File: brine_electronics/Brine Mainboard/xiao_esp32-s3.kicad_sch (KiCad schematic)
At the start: 4 parts, among them U1 XIAO-ESP32-S3-SMD

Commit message: Updated electronics/enclosure designs
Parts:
- removed H3: Antenna, MountingHole:MountingHole_3.2mm_M3, symbol Mechanical:MountingHole
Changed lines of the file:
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@@
-	)
-	(symbol
-		(lib_id "Mechanical:MountingHole")
-		(at 114.3 127 0)
-		(unit 1)
-		(exclude_from_sim yes)
-		(in_bom no)
-		(on_board yes)
-		(dnp no)
-		(fields_autoplaced yes)
-		(property "Reference" "H3"
-			(at 116.84 125.7299 0)
-			(effects
-				(font
-					(size 1.27 1.27)
-				)
-				(justify left)
-			)
-		)
-		(property "Value" "Antenna"
-			(at 116.84 128.2699 0)
-			(effects
-				(font
-					(size 1.27 1.27)
-				)
-				(justify left)
-			)
-		)
-		(property "Footprint" "MountingHole:MountingHole_3.2mm_M3"
-			(at 114.3 127 0)
-			(effects
-				(font
-					(size 1.27 1.27)
-				)
-				(hide yes)
-			)
-		)
-		(property "Datasheet" "~"
-			(at 114.3 127 0)
-			(effects
-				(font
-					(size 1.27 1.27)
-				)
-				(hide yes)
-			)
-		)
-		(property "Description" "Mounting Hole without connection"
-			(at 114.3 127 0)
-			(effects
-				(font
-					(size 1.27 1.27)
-				)
-				(hide yes)
-			)
-		)
-		(instances
-			(project "Brine"
-				(path "/da3a4ef2-0e38-46f1-a1fc-55d8e0a83a54/63bc593b-afd3-4a61-9e23-7e85a1d104e9"
-					(reference "H3")
-					(unit 1)
-				)
-			)
-		)
 	)
 	(symbol

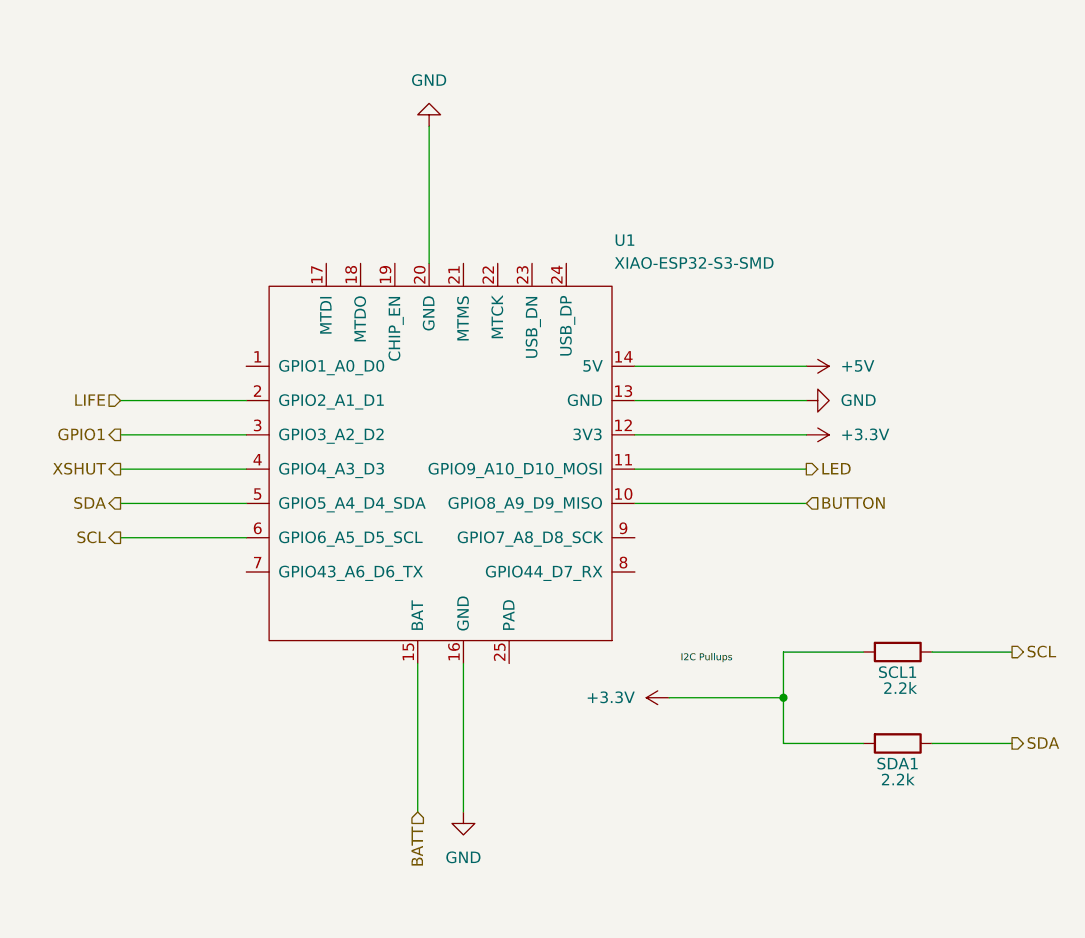
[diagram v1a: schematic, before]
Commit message: Implemented power latch circuit ⚡
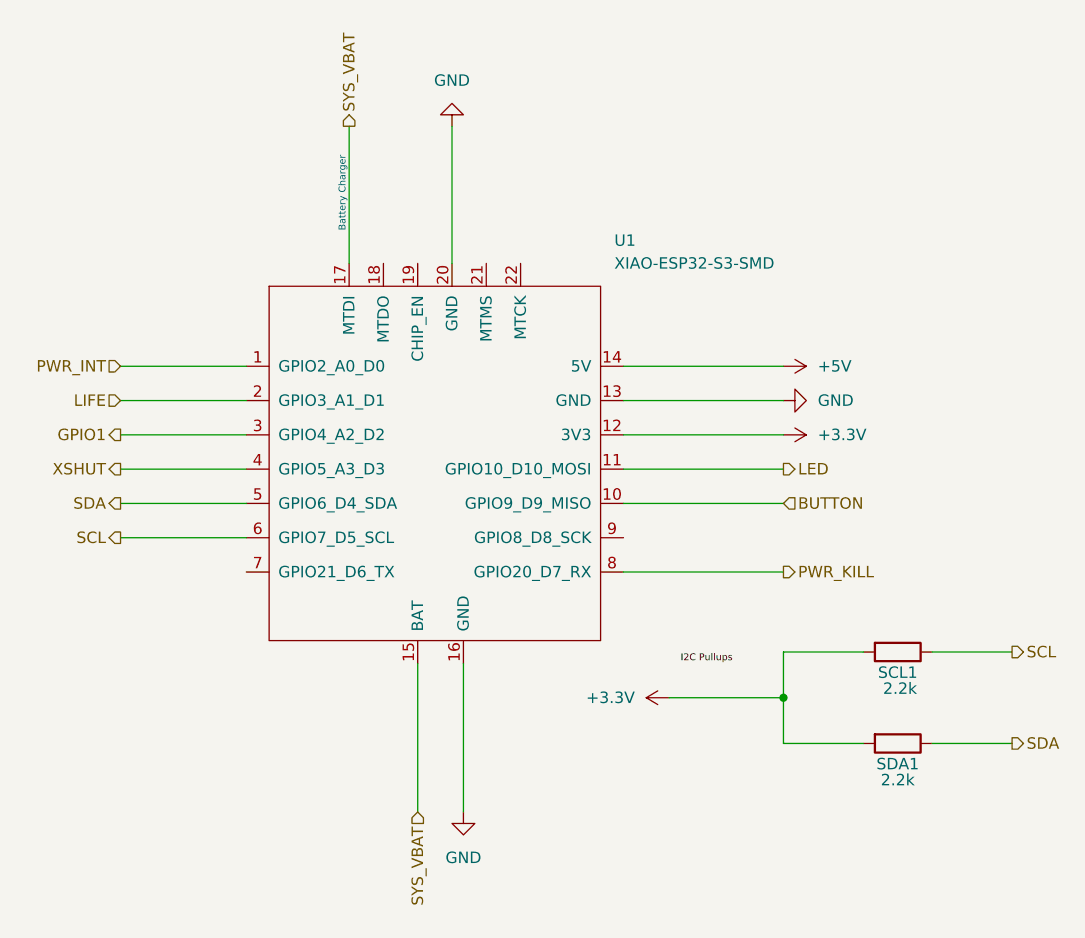
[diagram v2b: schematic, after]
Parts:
- U1: symbol Seeed_Studio_XIAO_Series:XIAO-ESP32-S3-SMD -> Seeed_Studio_XIAO_Series:XIAO-ESP32-C3-SMD
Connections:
- net BATT is gone; now on net SYS_VBAT: U1.15 (BAT)
- net PWR_INT: now reaches U1.1 (GPIO2_A0_D0)
- net SYS_VBAT: now reaches U1.17 (MTDI)
- net PWR_KILL: now reaches U1.8 (GPIO20_D7_RX)
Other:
- note added: "Battery Charger"
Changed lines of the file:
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@@
 		(comment 2 "The module incorporates a battery charger.")
+	)
+	(text "Battery Charger"
+		(exclude_from_sim no)
+		(at 128.778 71.12 90)
+		(effects
+			(font
+				(size 0.762 0.762)
+			)
+		)
 	)
 	(junction
@@
 	(wire
 		(pts
-			(xy 161.29 101.6) (xy 180.34 101.6)
-		)
-		(stroke
-			(width 0)
-			(type default)
-		)
-	)
-	(wire
-		(pts
 			(xy 142.24 123.19) (xy 142.24 139.7)
 		)
@@
 	(wire
 		(pts
-			(xy 161.29 105.41) (xy 180.34 105.41)
+			(xy 160.02 101.6) (xy 177.8 101.6)
+		)
+		(stroke
+			(width 0)
+			(type default)
+		)
+	)
+	(wire
+		(pts
+			(xy 160.02 93.98) (xy 177.8 93.98)
+		)
+		(stroke
+			(width 0)
+			(type default)
+		)
+	)
+	(wire
+		(pts
+			(xy 160.02 113.03) (xy 177.8 113.03)
 		)
 		(stroke
@@
 	(wire
 		(pts
-			(xy 161.29 93.98) (xy 180.34 93.98)
-		)
-		(stroke
-			(width 0)
-			(type default)
-		)
-	)
-	(wire
-		(pts
 			(xy 104.14 101.6) (xy 118.11 101.6)
 		)
@@
 	(wire
 		(pts
-			(xy 138.43 63.5) (xy 138.43 78.74)
+			(xy 140.97 63.5) (xy 140.97 78.74)
 		)
 		(stroke
@@
 	(wire
 		(pts
-			(xy 161.29 90.17) (xy 180.34 90.17)
+			(xy 129.54 63.5) (xy 129.54 78.74)
+		)
+		(stroke
+			(width 0)
+			(type default)
+		)
+	)
+	(wire
+		(pts
+			(xy 160.02 90.17) (xy 177.8 90.17)
+		)
+		(stroke
+			(width 0)
+			(type default)
+		)
+	)
+	(wire
+		(pts
+			(xy 104.14 90.17) (xy 118.11 90.17)
 		)
 		(stroke
@@
 	(wire
 		(pts
-			(xy 161.29 97.79) (xy 180.34 97.79)
+			(xy 160.02 97.79) (xy 177.8 97.79)
+		)
+		(stroke
+			(width 0)
+			(type default)
+		)
+	)
+	(wire
+		(pts
+			(xy 160.02 105.41) (xy 177.8 105.41)
 		)
 		(stroke
@@
 	(hierarchical_label "BUTTON"
 		(shape input)
-		(at 180.34 105.41 0)
+		(at 177.8 105.41 0)
 		(effects
 			(font
@@
 		)
 	)
+	(hierarchical_label "PWR_INT"
+		(shape input)
+		(at 104.14 90.17 180)
+		(effects
+			(font
+				(size 1.27 1.27)
+			)
+			(justify right)
+		)
+	)
 	(hierarchical_label "GPIO1"
 		(shape output)
@@
 		)
 	)
+	(hierarchical_label "SYS_VBAT"
+		(shape output)
+		(at 129.54 63.5 90)
+		(effects
+			(font
+				(size 1.27 1.27)
+			)
+			(justify left)
+		)
+	)
+	(hierarchical_label "PWR_KILL"
+		(shape output)
+		(at 177.8 113.03 0)
+		(effects
+			(font
+				(size 1.27 1.27)
+			)
+			(justify left)
+		)
+	)
 	(hierarchical_label "SCL"
 		(shape output)
@@
 		)
 	)
-	(hierarchical_label "BATT"
+	(hierarchical_label "SYS_VBAT"
 		(shape input)
 		(at 137.16 139.7 270)
@@
 	(hierarchical_label "LED"
 		(shape output)
-		(at 180.34 101.6 0)
+		(at 177.8 101.6 0)
 		(effects
 			(font
@@
 	)
 	(symbol
-		(lib_id "Seeed_Studio_XIAO_Series:XIAO-ESP32-S3-SMD")
+		(lib_id "Seeed_Studio_XIAO_Series:XIAO-ESP32-C3-SMD")
 		(at 139.7 101.6 0)
 		(unit 1)
@@
 		(pin "13"
 		)
-		(pin "23"
-		)
 		(pin "16"
 		)
@@
 		(pin "14"
 		)
-		(pin "24"
-		)
 		(pin "21"
 		)
@@
 		)
 		(pin "11"
-		)
-		(pin "25"
 		)
 		(instances
@@
 	(symbol
 		(lib_id "power:+3.3V")
-		(at 180.34 97.79 270)
+		(at 177.8 97.79 270)
 		(unit 1)
 		(exclude_from_sim no)
@@
 		(fields_autoplaced yes)
 		(property "Reference" "#PWR03"
-			(at 176.53 97.79 0)
+			(at 173.99 97.79 0)
 			(effects
 				(font
@@
 		)
 		(property "Value" "+3.3V"
-			(at 184.15 97.7899 90)
+			(at 181.61 97.7899 90)
 			(effects
 				(font
@@
 		)
 		(property "Footprint" ""
-			(at 180.34 97.79 0)
+			(at 177.8 97.79 0)
 			(effects
 				(font
@@
 		)
 		(property "Datasheet" ""
-			(at 180.34 97.79 0)
+			(at 177.8 97.79 0)
 			(effects
 				(font
@@
 		)
 		(property "Description" "Power symbol creates a global label with name \"+3.3V\""
-			(at 180.34 97.79 0)
+			(at 177.8 97.79 0)
 			(effects
 				(font
@@
 	(symbol
 		(lib_id "power:+5V")
-		(at 180.34 90.17 270)
+		(at 177.8 90.17 270)
 		(unit 1)
 		(exclude_from_sim no)
@@
 		(fields_autoplaced yes)
 		(property "Reference" "#PWR010"
-			(at 176.53 90.17 0)
+			(at 173.99 90.17 0)
 			(effects
 				(font
@@
 		)
 		(property "Value" "+5V"
-			(at 184.15 90.1699 90)
+			(at 181.61 90.1699 90)
 			(effects
 				(font
@@
 		)
 		(property "Footprint" ""
-			(at 180.34 90.17 0)
+			(at 177.8 90.17 0)
 			(effects
 				(font
@@
 		)
 		(property "Datasheet" ""
-			(at 180.34 90.17 0)
+			(at 177.8 90.17 0)
 			(effects
 				(font
@@
 		)
 		(property "Description" "Power symbol creates a global label with name \"+5V\""
-			(at 180.34 90.17 0)
+			(at 177.8 90.17 0)
 			(effects
 				(font
@@
 	(symbol
 		(lib_id "power:GND")
-		(at 138.43 63.5 180)
+		(at 140.97 63.5 180)
 		(unit 1)
 		(exclude_from_sim no)
@@
 		(fields_autoplaced yes)
 		(property "Reference" "#PWR04"
-			(at 138.43 57.15 0)
+			(at 140.97 57.15 0)
 			(effects
 				(font
@@
 		)
 		(property "Value" "GND"
-			(at 138.43 58.42 0)
+			(at 140.97 58.42 0)
 			(effects
 				(font
@@
 		)
 		(property "Footprint" ""
-			(at 138.43 63.5 0)
+			(at 140.97 63.5 0)
 			(effects
 				(font
@@
 		)
 		(property "Datasheet" ""
-			(at 138.43 63.5 0)
+			(at 140.97 63.5 0)
 			(effects
 				(font
@@
 		)
 		(property "Description" "Power symbol creates a global label with name \"GND\" , ground"
-			(at 138.43 63.5 0)
+			(at 140.97 63.5 0)
 			(effects
 				(font
@@
 	(symbol
 		(lib_id "power:GND")
-		(at 180.34 93.98 90)
+		(at 177.8 93.98 90)
 		(unit 1)
 		(exclude_from_sim no)
@@
 		(fields_autoplaced yes)
 		(property "Reference" "#PWR02"
-			(at 186.69 93.98 0)
+			(at 184.15 93.98 0)
 			(effects
 				(font
@@
 		)
 		(property "Value" "GND"
-			(at 184.15 93.9799 90)
+			(at 181.61 93.9799 90)
 			(effects
 				(font
@@
 		)
 		(property "Footprint" ""
-			(at 180.34 93.98 0)
+			(at 177.8 93.98 0)
 			(effects
 				(font
@@
 		)
 		(property "Datasheet" ""
-			(at 180.34 93.98 0)
+			(at 177.8 93.98 0)
 			(effects
 				(font
@@
 		)
 		(property "Description" "Power symbol creates a global label with name \"GND\" , ground"
-			(at 180.34 93.98 0)
-			(effects
-				(font
+			(at 177.8 93.98 0)
+			(effects
+				(font

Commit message: Resolved schematic DRC issues ✅
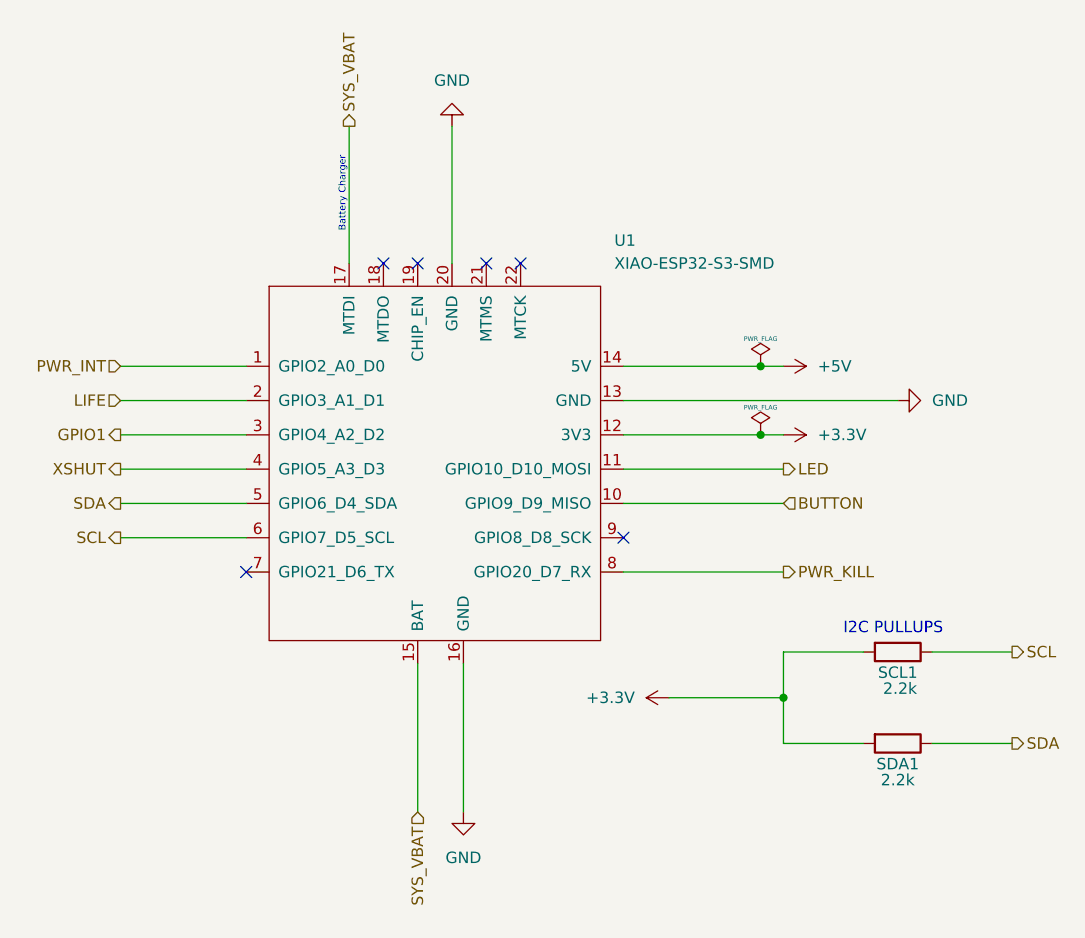
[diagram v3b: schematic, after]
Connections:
- no-connect marks 0 -> 6
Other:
- note added: "I2C PULLUPS"
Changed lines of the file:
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@@
 	(title_block
 		(title "Brine - XIAO ESP32-S3")
-		(date "2026-04-03")
+		(date "2026-04-07")
 		(rev "1.0.0")
 		(company "Splendid Endeavors")
@@
 		(comment 2 "The module incorporates a battery charger.")
 	)
+	(text "I2C PULLUPS"
+		(exclude_from_sim no)
+		(at 189.992 119.38 0)
+		(effects
+			(font
+				(size 1.27 1.27)
+			)
+		)
+	)
 	(text "Battery Charger"
 		(exclude_from_sim no)
@@
 			)
 		)
+	)
+	(junction
+		(at 175.26 90.17)
+		(diameter 0)
+		(color 0 0 0 0)
+	)
+	(junction
+		(at 175.26 97.79)
+		(diameter 0)
+		(color 0 0 0 0)
 	)
 	(junction
@@
 		(color 0 0 0 0)
 	)
+	(no_connect
+		(at 148.59 78.74)
+	)
+	(no_connect
+		(at 137.16 78.74)
+	)
+	(no_connect
+		(at 160.02 109.22)
+	)
+	(no_connect
+		(at 118.11 113.03)
+	)
+	(no_connect
+		(at 144.78 78.74)
+	)
+	(no_connect
+		(at 133.35 78.74)
+	)
 	(wire
 		(pts
@@
 	(wire
 		(pts
-			(xy 160.02 93.98) (xy 177.8 93.98)
+			(xy 160.02 93.98) (xy 190.5 93.98)
 		)
 		(stroke
@@
 	(wire
 		(pts
+			(xy 175.26 90.17) (xy 177.8 90.17)
+		)
+		(stroke
+			(width 0)
+			(type default)
+		)
+	)
+	(wire
+		(pts
 			(xy 104.14 93.98) (xy 118.11 93.98)
 		)
@@
 	(wire
 		(pts
-			(xy 160.02 90.17) (xy 177.8 90.17)
+			(xy 175.26 97.79) (xy 177.8 97.79)
+		)
+		(stroke
+			(width 0)
+			(type default)
+		)
+	)
+	(wire
+		(pts
+			(xy 160.02 90.17) (xy 175.26 90.17)
 		)
 		(stroke
@@
 	(wire
 		(pts
-			(xy 160.02 97.79) (xy 177.8 97.79)
+			(xy 160.02 97.79) (xy 175.26 97.79)
 		)
 		(stroke
@@
 			(width 0)
 			(type default)
-		)
-	)
-	(label "I2C Pullups"
-		(at 166.37 123.19 0)
-		(effects
-			(font
-				(size 0.762 0.762)
-			)
-			(justify left bottom)
 		)
 	)
@@
 	)
 	(symbol
+		(lib_id "power:PWR_FLAG")
+		(at 175.26 90.17 0)
+		(unit 1)
+		(exclude_from_sim no)
+		(in_bom yes)
+		(on_board yes)
+		(dnp no)
+		(property "Reference" "#FLG01"
+			(at 175.26 88.265 0)
+			(effects
+				(font
+					(size 1.27 1.27)
+				)
+				(hide yes)
+			)
+		)
+		(property "Value" "PWR_FLAG"
+			(at 175.26 87.122 0)
+			(effects
+				(font
+					(size 0.508 0.508)
+				)
+			)
+		)
+		(property "Footprint" ""
+			(at 175.26 90.17 0)
+			(effects
+				(font
+					(size 1.27 1.27)
+				)
+				(hide yes)
+			)
+		)
+		(property "Datasheet" "~"
+			(at 175.26 90.17 0)
+			(effects
+				(font
+					(size 1.27 1.27)
+				)
+				(hide yes)
+			)
+		)
+		(property "Description" "Special symbol for telling ERC where power comes from"
+			(at 175.26 90.17 0)
+			(effects
+				(font
+					(size 1.27 1.27)
+				)
+				(hide yes)
+			)
+		)
+		(pin "1"
+		)
+		(instances
+			(project ""
+				(path "/da3a4ef2-0e38-46f1-a1fc-55d8e0a83a54/63bc593b-afd3-4a61-9e23-7e85a1d104e9"
+					(reference "#FLG01")
+					(unit 1)
+				)
+			)
+		)
+	)
+	(symbol
 		(lib_id "power:+5V")
 		(at 177.8 90.17 270)
@@
 	)
 	(symbol
+		(lib_id "power:PWR_FLAG")
+		(at 175.26 97.79 0)
+		(unit 1)
+		(exclude_from_sim no)
+		(in_bom yes)
+		(on_board yes)
+		(dnp no)
+		(property "Reference" "#FLG02"
+			(at 175.26 95.885 0)
+			(effects
+				(font
+					(size 1.27 1.27)
+				)
+				(hide yes)
+			)
+		)
+		(property "Value" "PWR_FLAG"
+			(at 175.26 94.742 0)
+			(effects
+				(font
+					(size 0.508 0.508)
+				)
+			)
+		)
+		(property "Footprint" ""
+			(at 175.26 97.79 0)
+			(effects
+				(font
+					(size 1.27 1.27)
+				)
+				(hide yes)
+			)
+		)
+		(property "Datasheet" "~"
+			(at 175.26 97.79 0)
+			(effects
+				(font
+					(size 1.27 1.27)
+				)
+				(hide yes)
+			)
+		)
+		(property "Description" "Special symbol for telling ERC where power comes from"
+			(at 175.26 97.79 0)
+			(effects
+				(font
+					(size 1.27 1.27)
+				)
+				(hide yes)
+			)
+		)
+		(pin "1"
+		)
+		(instances
+			(project ""
+				(path "/da3a4ef2-0e38-46f1-a1fc-55d8e0a83a54/63bc593b-afd3-4a61-9e23-7e85a1d104e9"
+					(reference "#FLG02")
+					(unit 1)
+				)
+			)
+		)
+	)
+	(symbol
 		(lib_id "power:GND")
-		(at 177.8 93.98 90)
+		(at 190.5 93.98 90)
 		(unit 1)
 		(exclude_from_sim no)
@@
 		(fields_autoplaced yes)
 		(property "Reference" "#PWR02"
-			(at 184.15 93.98 0)
+			(at 196.85 93.98 0)
 			(effects
 				(font
@@
 		)
 		(property "Value" "GND"
-			(at 181.61 93.9799 90)
+			(at 194.31 93.9799 90)
 			(effects
 				(font
@@
 		)
 		(property "Footprint" ""
-			(at 177.8 93.98 0)
+			(at 190.5 93.98 0)
 			(effects
 				(font
@@
 		)
 		(property "Datasheet" ""
-			(at 177.8 93.98 0)
+			(at 190.5 93.98 0)
 			(effects
 				(font
@@
 		)
 		(property "Description" "Power symbol creates a global label with name \"GND\" , ground"
-			(at 177.8 93.98 0)
-			(effects
-				(font
+			(at 190.5 93.98 0)
+			(effects
+				(font
